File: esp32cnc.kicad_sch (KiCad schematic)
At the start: 25 parts, among them J1 Barrel_Jack, J2 USB_B_Micro, J3 Micro_SD_Card_Det1, J4 Screw_Terminal_01x04, J5 Screw_Terminal_01x04, J6 Screw_Terminal_01x04, J7 Screw_Terminal_01x02, U1 ESP32-WROOM-32, U2 OKI-78SR-3.3_1.5-W36-C, U3 CH330N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

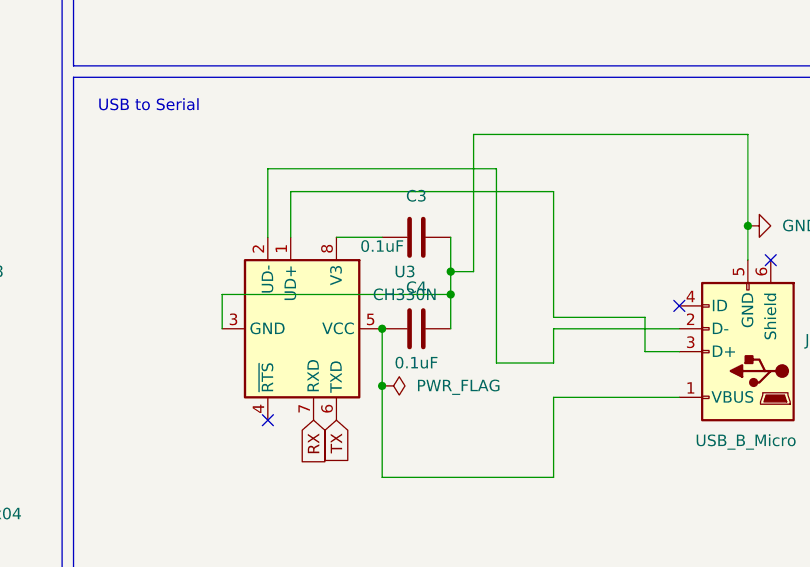
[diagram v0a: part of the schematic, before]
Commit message: change to ch340n
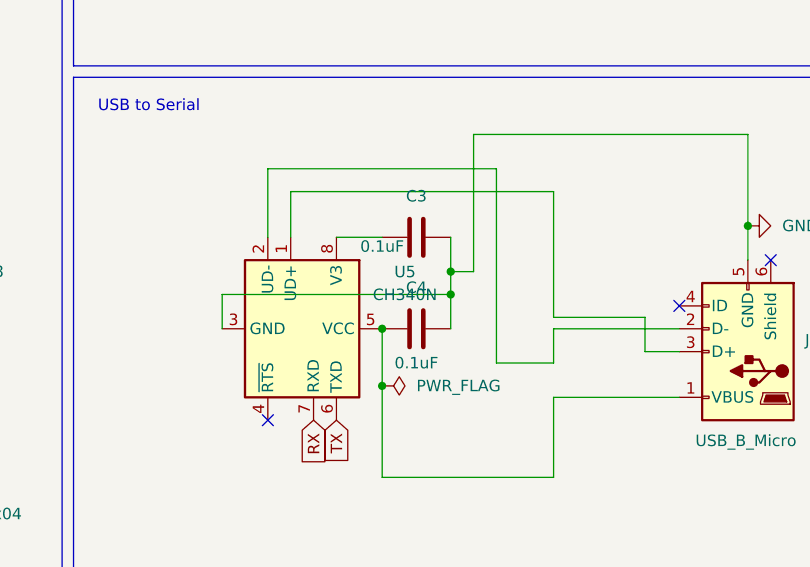
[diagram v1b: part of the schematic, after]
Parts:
- removed U3: CH330N, Package_SO:SOIC-8_3.9x4.9mm_P1.27mm, symbol Interface_USB:CH330N
- added U5: CH340N, Package_SO:SOP-8_3.9x4.9mm_P1.27mm, symbol Interface_USB:CH340N
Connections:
- net GND: now also U5.3 (GND)
- net RX: now also U5.7 (RXD)
- net TX: now also U5.6 (TXD)
- net at C4.2, J2.1 (VBUS): now also U5.5 (VCC)
- net at J2.2 (D-): now also U5.2 (UD-)
- net at J2.3 (D+): now also U5.1 (UD+)
- net at C3.2: now also U5.8 (V3)
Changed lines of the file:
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@@
 	)
 	(junction
+		(at 232.41 97.79)
+		(diameter 0)
+		(color 0 0 0 0)
+	)
+	(junction
 		(at 35.56 143.51)
 		(diameter 0)
@@
 	)
 	(junction
-		(at 232.41 97.79)
-		(diameter 0)
-		(color 0 0 0 0)
-	)
-	(junction
 		(at 240.03 93.98)
 		(diameter 0)
@@
 	)
 	(symbol
+		(lib_id "Interface_USB:CH340N")
+		(at 224.79 97.79 270)
+		(unit 1)
+		(exclude_from_sim no)
+		(in_bom yes)
+		(on_board yes)
+		(dnp no)
+		(fields_autoplaced yes)
+		(property "Reference" "U5"
+			(at 234.95 91.4714 90)
+			(effects
+				(font
+					(size 1.27 1.27)
+				)
+			)
+		)
+		(property "Value" "CH340N"
+			(at 234.95 94.0114 90)
+			(effects
+				(font
+					(size 1.27 1.27)
+				)
+			)
+		)
+		(property "Footprint" "Package_SO:SOP-8_3.9x4.9mm_P1.27mm"
+			(at 243.84 93.98 0)
+			(effects
+				(font
+					(size 1.27 1.27)
+				)
+				(hide yes)
+			)
+		)
+		(property "Datasheet" "https://aitendo3.sakura.ne.jp/aitendo_data/product_img/ic/inteface/CH340N/ch340n.pdf"
+			(at 229.87 95.25 0)
+			(effects
+				(font
+					(size 1.27 1.27)
+				)
+				(hide yes)
+			)
+		)
+		(property "Description" "USB serial converter, 2Mbps, UART, SOP-8"
+			(at 224.79 97.79 0)
+			(effects
+				(font
+					(size 1.27 1.27)
+				)
+				(hide yes)
+			)
+		)
+		(pin "3"
+		)
+		(pin "1"
+		)
+		(pin "6"
+		)
+		(pin "5"
+		)
+		(pin "4"
+		)
+		(pin "7"
+		)
+		(pin "2"
+		)
+		(pin "8"
+		)
+		(instances
+			(project ""
+				(path "/7af93405-7672-4ec9-bf48-095aefb21bf3"
+					(reference "U5")
+					(unit 1)
+				)
+			)
+		)
+	)
+	(symbol
 		(lib_id "power:GND")
 		(at 35.56 135.89 180)
@@
 					(unit 1)
 				)
-			)
-		)
-	)
-	(symbol
-		(lib_id "Interface_USB:CH330N")
-		(at 224.79 97.79 270)
-		(unit 1)
-		(exclude_from_sim no)
-		(in_bom yes)
-		(on_board yes)
-		(dnp no)
-		(fields_autoplaced yes)
-		(property "Reference" "U3"
-			(at 234.95 91.4714 90)
-			(effects
-				(font
-					(size 1.27 1.27)
-				)
-			)
-		)
-		(property "Value" "CH330N"
-			(at 234.95 94.0114 90)
-			(effects
-				(font
-					(size 1.27 1.27)
-				)
-			)
-		)
-		(property "Footprint" "Package_SO:SOIC-8_3.9x4.9mm_P1.27mm"
-			(at 243.84 93.98 0)
-			(effects
-				(font
-					(size 1.27 1.27)
-				)
-				(hide yes)
-			)
-		)
-		(property "Datasheet" "http://www.wch.cn/downloads/file/240.html"
-			(at 229.87 95.25 0)
-			(effects
-				(font
-					(size 1.27 1.27)
-				)
-				(hide yes)
-			)
-		)
-		(property "Description" "USB serial converter, UART, SOIC-8"
-			(at 224.79 97.79 0)
-			(effects
-				(font
-					(size 1.27 1.27)
-				)
-				(hide yes)
-			)
-		)
-		(pin "2"
-		)
-		(pin "4"
-		)
-		(pin "7"
-		)
-		(pin "5"
-		)
-		(pin "3"
-		)
-		(pin "6"
-		)
-		(pin "8"
-		)
-		(pin "1"
-		)
-		(instances
-			(project "esp32cnc"
-				(path "/7af93405-7672-4ec9-bf48-095aefb21bf3"
-					(reference "U3")
-					(unit 1)
-				)

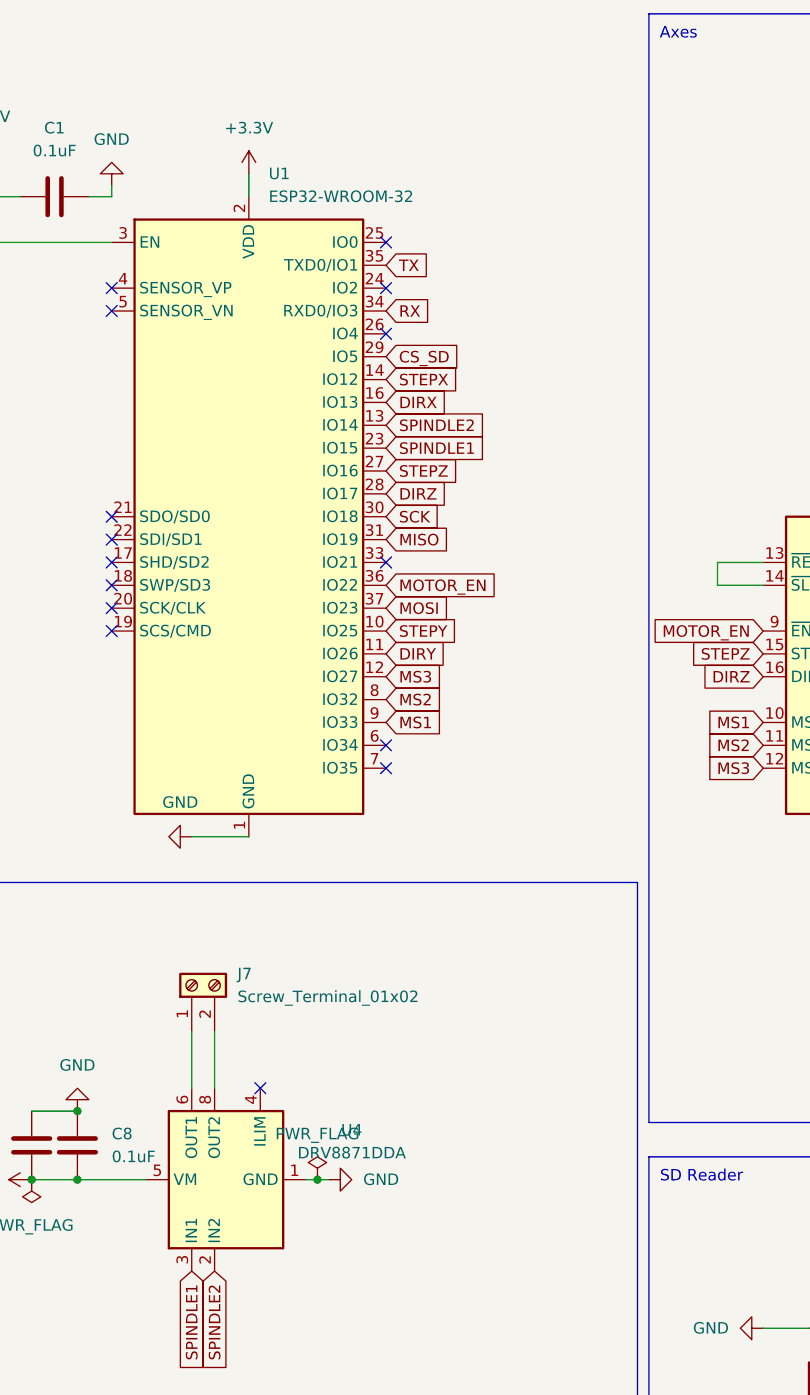
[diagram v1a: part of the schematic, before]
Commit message: flipped rx/tx, added boot button, added ILM resistor
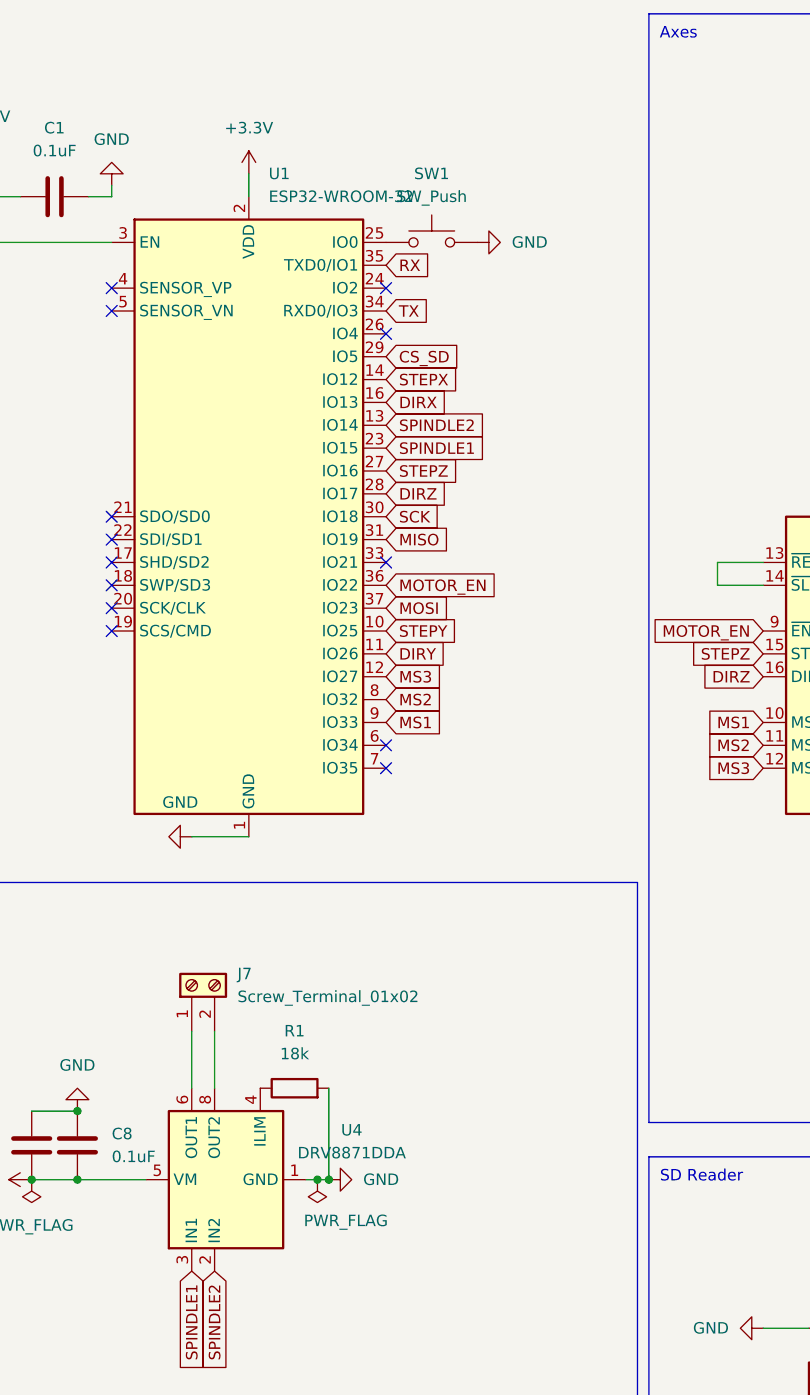
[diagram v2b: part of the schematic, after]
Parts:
- added R1: 18k, symbol Device:R
- added SW1: SW_Push, symbol Switch:SW_Push
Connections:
- net GND: now also R1.2, SW1.2
- net RX: now also U1.35 (TXD0/IO1); no longer U1.34 (RXD0/IO3)
- net TX: now also U1.34 (RXD0/IO3); no longer U1.35 (TXD0/IO1)
- net at U1.25 (IO0): now also SW1.1
- net at U4.4 (ILIM): now also R1.1
- no-connect marks 21 -> 19
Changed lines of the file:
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@@
 	(title_block
 		(title "DIY CNC Board")
-		(date "2024-11-11")
-		(rev "2")
+		(date "2025-01-23")
+		(rev "3")
 		(company "Pengalu")
 		(comment 1 "github.com/Pengalu")
@@
 	)
 	(junction
+		(at 63.5 143.51)
+		(diameter 0)
+		(color 0 0 0 0)
+	)
+	(junction
 		(at 240.03 91.44)
 		(diameter 0)
@@
 	)
 	(no_connect
-		(at 55.88 133.35)
-	)
-	(no_connect
 		(at 39.37 80.01)
 	)
-	(no_connect
-		(at 69.85 39.37)
-	)
 	(wire
 		(pts
@@
 	(wire
 		(pts
+			(xy 63.5 133.35) (xy 63.5 143.51)
+		)
+		(stroke
+			(width 0)
+			(type default)
+		)
+	)
+	(wire
+		(pts
 			(xy 162.56 129.54) (xy 167.64 129.54)
 		)
@@
 	(global_label "RX"
 		(shape input)
-		(at 69.85 46.99 0)
+		(at 69.85 41.91 0)
 		(fields_autoplaced yes)
 		(effects
@@
 		)
 		(property "Intersheetrefs" "${INTERSHEET_REFS}"
-			(at 75.3147 46.99 0)
+			(at 75.3147 41.91 0)
 			(effects
 				(font
@@
 	(global_label "TX"
 		(shape input)
-		(at 69.85 41.91 0)
+		(at 69.85 46.99 0)
 		(fields_autoplaced yes)
 		(effects
@@
 		)
 		(property "Intersheetrefs" "${INTERSHEET_REFS}"
-			(at 75.0123 41.91 0)
+			(at 75.0123 46.99 0)
 			(effects
 				(font
@@
 	)
 	(symbol
+		(lib_id "Switch:SW_Push")
+		(at 74.93 39.37 0)
+		(unit 1)
+		(exclude_from_sim no)
+		(in_bom yes)
+		(on_board yes)
+		(dnp no)
+		(fields_autoplaced yes)
+		(property "Reference" "SW1"
+			(at 74.93 31.75 0)
+			(effects
+				(font
+					(size 1.27 1.27)
+				)
+			)
+		)
+		(property "Value" "SW_Push"
+			(at 74.93 34.29 0)
+			(effects
+				(font
+					(size 1.27 1.27)
+				)
+			)
+		)
+		(property "Footprint" ""
+			(at 74.93 34.29 0)
+			(effects
+				(font
+					(size 1.27 1.27)
+				)
+				(hide yes)
+			)
+		)
+		(property "Datasheet" "~"
+			(at 74.93 34.29 0)
+			(effects
+				(font
+					(size 1.27 1.27)
+				)
+				(hide yes)
+			)
+		)
+		(property "Description" "Push button switch, generic, two pins"
+			(at 74.93 39.37 0)
+			(effects
+				(font
+					(size 1.27 1.27)
+				)
+				(hide yes)
+			)
+		)
+		(pin "2"
+		)
+		(pin "1"
+		)
+		(instances
+			(project ""
+				(path "/7af93405-7672-4ec9-bf48-095aefb21bf3"
+					(reference "SW1")
+					(unit 1)
+				)
+			)
+		)
+	)
+	(symbol
 		(lib_id "Connector:Screw_Terminal_01x04")
 		(at 182.88 49.53 0)
@@
 	)
 	(symbol
+		(lib_id "power:GND")
+		(at 80.01 39.37 90)
+		(unit 1)
+		(exclude_from_sim no)
+		(in_bom yes)
+		(on_board yes)
+		(dnp no)
+		(fields_autoplaced yes)
+		(property "Reference" "#PWR028"
+			(at 86.36 39.37 0)
+			(effects
+				(font
+					(size 1.27 1.27)
+				)
+				(hide yes)
+			)
+		)
+		(property "Value" "GND"
+			(at 83.82 39.3699 90)
+			(effects
+				(font
+					(size 1.27 1.27)
+				)
+				(justify right)
+			)
+		)
+		(property "Footprint" ""
+			(at 80.01 39.37 0)
+			(effects
+				(font
+					(size 1.27 1.27)
+				)
+				(hide yes)
+			)
+		)
+		(property "Datasheet" ""
+			(at 80.01 39.37 0)
+			(effects
+				(font
+					(size 1.27 1.27)
+				)
+				(hide yes)
+			)
+		)
+		(property "Description" "Power symbol creates a global label with name \"GND\" , ground"
+			(at 80.01 39.37 0)
+			(effects
+				(font
+					(size 1.27 1.27)
+				)
+				(hide yes)
+			)
+		)
+		(pin "1"
+		)
+		(instances
+			(project ""
+				(path "/7af93405-7672-4ec9-bf48-095aefb21bf3"
+					(reference "#PWR028")
+					(unit 1)
+				)
+			)
+		)
+	)
+	(symbol
 		(lib_id "power:+12V")
 		(at 167.64 21.59 0)
@@
 	(symbol
 		(lib_id "power:PWR_FLAG")
-		(at 62.23 143.51 0)
+		(at 62.23 143.51 180)
 		(unit 1)
 		(exclude_from_sim no)
@@
 		(on_board yes)
 		(dnp no)
-		(fields_autoplaced yes)
 		(property "Reference" "#FLG03"
-			(at 62.23 141.605 0)
+			(at 62.23 145.415 0)
 			(effects
 				(font
@@
 		)
 		(property "Value" "PWR_FLAG"
-			(at 62.23 138.43 0)
+			(at 60.706 148.082 0)
 			(effects
 				(font
 					(size 1.27 1.27)
 				)
+				(justify right)
 			)
 		)
@@
 					(unit 1)
 				)
+			)
+		)
+	)
+	(symbol
+		(lib_id "Device:R")
+		(at 59.69 133.35 90)
+		(unit 1)
+		(exclude_from_sim no)
+		(in_bom yes)
+		(on_board yes)
+		(dnp no)
+		(fields_autoplaced yes)
+		(property "Reference" "R1"
+			(at 59.69 127 90)
+			(effects
+				(font
+					(size 1.27 1.27)
+				)
+			)
+		)
+		(property "Value" "18k"
+			(at 59.69 129.54 90)
+			(effects
+				(font
+					(size 1.27 1.27)
+				)
+			)
+		)
+		(property "Footprint" ""
+			(at 59.69 135.128 90)
+			(effects
+				(font
+					(size 1.27 1.27)
+				)
+				(hide yes)
+			)
+		)
+		(property "Datasheet" "~"
+			(at 59.69 133.35 0)
+			(effects
+				(font
+					(size 1.27 1.27)
+				)
+				(hide yes)
+			)
+		)
+		(property "Description" "Resistor"
+			(at 59.69 133.35 0)
+			(effects
+				(font
+					(size 1.27 1.27)
+				)
+				(hide yes)
+			)
+		)
+		(pin "2"
+		)
+		(pin "1"
+		)
+		(instances
+			(project ""
+				(path "/7af93405-7672-4ec9-bf48-095aefb21bf3"
+					(reference "R1")
+					(unit 1)
+				)
